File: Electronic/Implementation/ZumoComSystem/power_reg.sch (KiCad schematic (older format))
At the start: 16 parts, among them Q1 PMOS-RQ5C060BCTCL, SW1 MLL1200S, U1 LT1374CS8-5PBF, U2 TPS62056DGS

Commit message: Coutouts, BOM, ...
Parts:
- removed Q1: PMOS-RQ5C060BCTCL, footprints:SOT95P280X100-3N, symbol Device:Q_PMOS_GDS
- added Q1: PMOS_GSD-RQ5C060BCTCL, footprints:SOT95P280X100-3N, symbol Device:Q_PMOS_GSD
- C1, C3, C4: Manufacturer (none) -> TDK Corporation; Part-No. (none) -> C3216X5R1V226M160AC
- C2: Manufacturer (none) -> TDK Corporation; Part-No. (none) -> C2012X5R1V106M085AC
- C5: Manufacturer (none) -> KEMET; Part-No. (none) -> C0805C274K5RACTU
- C6: Manufacturer (none) -> TDK Corporation; Part-No. (none) -> C3216X5R1A107M160AC
- D1: Manufacturer (none) -> Kyocera AVX; Part-No. (none) -> SD2114S040S5R0
- D2: Manufacturer (none) -> SMC Diode Solutions; Part-No. (none) -> SD103BWSA
- L1: Manufacturer (none) -> Würth Elektronik; Part-No. (none) -> 74437368150
- L2: Manufacturer (none) -> Vishay Dale; Part-No. (none) -> IHLP6767GZER220M11
- R1: value 100k -> 10k; Manufacturer (none) -> TE Connectivity Passive Product; Part-No. (none) -> CRGCQ0603J10K
- R2: value 100k -> 68k; Manufacturer (none) -> TE Connectivity Passive Product; Part-No. (none) -> CRGCQ0603F68K
- SW1: Comment 1437575-1 -> (none); Manufacturer (none) -> TE Connectivity / P&B; Part-No. (none) -> MLL1200S
- U1: MANUFACTURER_PART_NUMBER lt1374cs85#pbf -> (none); Manufacturer (none) -> Analog Device; Part-No. (none) -> LT1374CS8-5PBF; VENDOR Linear Technology -> (none)
- U2: Manufacturer (none) -> Texas Instruments; Part-No. (none) -> TPS62056DGS

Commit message: replaced 3V3 Regulator
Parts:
- removed C3: 22uF, Capacitor_SMD:C_1206_3216Metric_Pad1.42x1.75mm_HandSolder, symbol Device:C
- removed U2: TPS62056DGS, SOP50P490X110-10N, symbol TPS62056DGS:TPS62056DGS
- added C6: 10u, Capacitor_SMD:C_0805_2012Metric_Pad1.15x1.40mm_HandSolder, symbol Device:C
- added R3: 10k, Resistor_SMD:R_0603_1608Metric_Pad1.05x0.95mm_HandSolder, symbol Device:R
- added U2: ADP2370ACPZ-3.3-R7, footprints:DFN300X300X80-9N_thermal, symbol 2022-04-19_08-29-50:ADP2370ACPZ-3.3-R7
- C2: value 10uF -> 10u
- L1: value 15uH -> 6.8u; footprint footprints:L_Wuerth_HCI-1040_3D -> Inductor_SMD:L_Coilcraft_XxL4040; Manufacturer Würth Elektronik -> Coilcraft; Part-No. 74437368150 -> XAL4030-682MEC
- renumbered C4 to C3, C5 to C4, C6 to C5
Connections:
- net +3V3: now also C6.1, U2.5 (FB)
- net GND: now also C6.2, U2.4 (SYNC), U2.8 (PGND), U2.9 (EPAD)
- net at C1.1, C2.1, C3.1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: now also R3.2, U2.1 (VIN), U2.2 (FSEL), U2.3 (EN)
- net at L1.1: now also U2.7 (SW)
- new net: R3.1, U2.6 (PG)
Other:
- note added: "Imax = 250mA"
- note removed: "Imax = 200 mA"
- moved on the sheet: L1

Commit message: actualized BOM
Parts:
- U2: Manufacturer (none) -> Analog Device; Part-No. (none) -> ADP2371ACPZ-3.3-R7
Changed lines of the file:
@@
 F 2 "footprints:DFN300X300X80-9N_thermal" H 6200 1640 60  0001 C CNN
 F 3 "https://www.analog.com/media/en/technical-documentation/data-sheets/ADP2370_2371.pdf" H 6200 1681 60  0001 C CNN
+F 4 "Analog Device" H 5000 1400 50  0001 C CNN "Manufacturer"
+F 5 "ADP2371ACPZ-3.3-R7" H 5000 1400 50  0001 C CNN "Part-No."
 	1    5000 1400
 	1    0    0    -1

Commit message: Electronic: ZumoCom System: finhished/ orderd PCB + add Version and TOP/BOT on PCB
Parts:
- C1: Manufacturer TDK Corporation -> Murata Electronics; Part-No. C3216X5R1V226M160AC -> GRM31CC81E226KE11L
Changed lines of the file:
@@
 Sheet 2 7
 Title "Zumo Communication System"
-Date "2022-04-22"
+Date "2022-05-13"
 Rev "V1.0"
 Comp "NewTec GmbH"
@@
 F 2 "Capacitor_SMD:C_1206_3216Metric_Pad1.42x1.75mm_HandSolder" H 3988 4700 50  0001 C CNN
 F 3 "https://product.tdk.com/info/en/catalog/datasheets/mlcc_commercial_general_en.pdf?ref_disty=digikey" H 3950 4850 50  0001 C CNN
-F 4 "TDK Corporation" H 3950 4850 50  0001 C CNN "Manufacturer"
-F 5 "C3216X5R1V226M160AC " H 3950 4850 50  0001 C CNN "Part-No."
+F 4 " Murata Electronics " H 3950 4850 50  0001 C CNN "Manufacturer"
+F 5 "GRM31CC81E226KE11L" H 3950 4850 50  0001 C CNN "Part-No."
 	1    3950 4850
 	1    0    0    -1

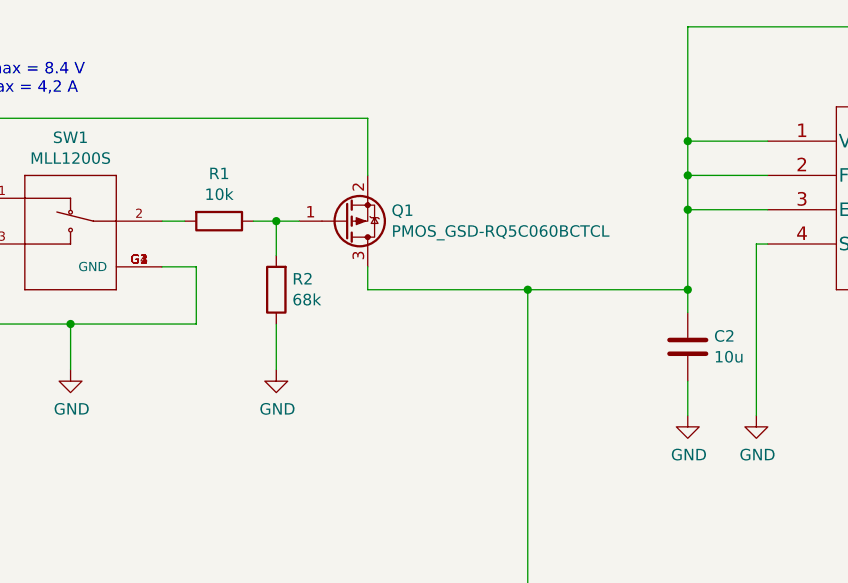
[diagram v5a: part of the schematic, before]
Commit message: #93 Voltage divider removed and another MOSFET Q1 selected
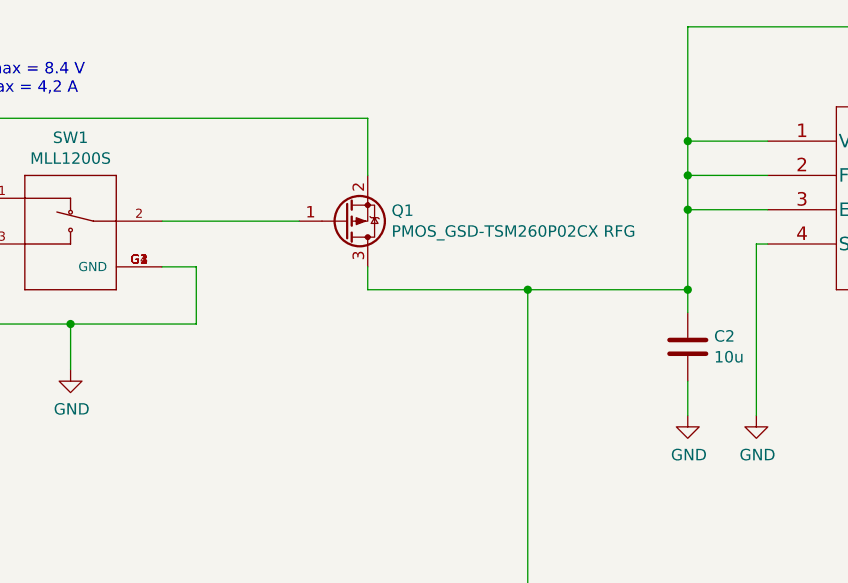
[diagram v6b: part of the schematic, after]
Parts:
- removed R1: 10k, Resistor_SMD:R_0603_1608Metric_Pad1.05x0.95mm_HandSolder, symbol Device:R
- removed R2: 68k, Resistor_SMD:R_0603_1608Metric_Pad1.05x0.95mm_HandSolder, symbol Device:R
- Q1: value PMOS_GSD-RQ5C060BCTCL -> PMOS_GSD-TSM260P02CX RFG; footprint footprints:SOT95P280X100-3N -> Package_TO_SOT_SMD:SOT-23_Handsoldering; Manufacturer Rohm Semiconductor -> Taiwan Semiconductor; Part-No. RQ5C060BCTCL -> TSM260P02CX RFG
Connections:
- net at SW1.2: now also Q1.1 (G)
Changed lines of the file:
@@
 	1000 1250 1450 1250
 Wire Wire Line
-	2350 1700 2450 1700
-Wire Wire Line
-	2750 1700 2850 1700
-Wire Wire Line
-	2850 2350 2850 2150
-Wire Wire Line
-	2850 1850 2850 1700
-$Comp
-L power:GND #PWR02
-U 1 1 62464A3F
-P 2850 2350
-F 0 "#PWR02" H 2850 2100 50  0001 C CNN
-F 1 "GND" H 2855 2177 50  0000 C CNN
-F 2 "" H 2850 2350 50  0001 C CNN
-F 3 "" H 2850 2350 50  0001 C CNN
-	1    2850 2350
-	1    0    0    -1
-$EndComp
-Wire Wire Line
 	3250 2000 3250 1900
 Wire Wire Line
 	3250 2000 3950 2000
-Wire Wire Line
-	2950 1700 2850 1700
-Connection ~ 2850 1700
 Wire Wire Line
 	3250 1250 3250 1500
@@
 $EndComp
 $Comp
-L Device:R R1
-U 1 1 62459142
-P 2600 1700
-F 0 "R1" V 2393 1700 50  0000 C CNN
-F 1 "10k" V 2484 1700 50  0000 C CNN
-F 2 "Resistor_SMD:R_0603_1608Metric_Pad1.05x0.95mm_HandSolder" V 2530 1700 50  0001 C CNN
-F 3 "~" H 2600 1700 50  0001 C CNN
-F 4 "TE Connectivity Passive Product" H 2600 1700 50  0001 C CNN "Manufacturer"
-F 5 "CRGCQ0603J10K" H 2600 1700 50  0001 C CNN "Part-No."
-	1    2600 1700
-	0    1    1    0
-$EndComp
-$Comp
-L Device:R R2
-U 1 1 6245A145
-P 2850 2000
-F 0 "R2" H 2780 1954 50  0000 R CNN
-F 1 "68k" H 2780 2045 50  0000 R CNN
-F 2 "Resistor_SMD:R_0603_1608Metric_Pad1.05x0.95mm_HandSolder" V 2780 2000 50  0001 C CNN
-F 3 "~" H 2850 2000 50  0001 C CNN
-F 4 "TE Connectivity Passive Product" H 2850 2000 50  0001 C CNN "Manufacturer"
-F 5 "CRGCQ0603F68K" H 2850 2000 50  0001 C CNN "Part-No."
-	1    2850 2000
-	-1   0    0    1
-$EndComp
-$Comp
 L Device:L L1
 U 1 1 60C698F7
@@
 P 3150 1700
 F 0 "Q1" H 3354 1654 50  0000 L CNN
-F 1 "PMOS_GSD-RQ5C060BCTCL" H 3354 1745 50  0000 L CNN
-F 2 "footprints:SOT95P280X100-3N" H 3350 1800 50  0001 C CNN
-F 3 "https://fscdn.rohm.com/en/products/databook/datasheet/discrete/transistor/mosfet/rq5c060bctcl-e.pdf" H 3150 1700 50  0001 C CNN
-F 4 "Rohm Semiconductor" H 3150 1700 50  0001 C CNN "Manufacturer"
-F 5 "RQ5C060BCTCL" H 3150 1700 50  0001 C CNN "Part-No."
+F 1 "PMOS_GSD-TSM260P02CX RFG " H 3354 1745 50  0000 L CNN
+F 2 "Package_TO_SOT_SMD:SOT-23_Handsoldering" H 3350 1800 50  0001 C CNN
+F 3 "https://www.mouser.de/datasheet/2/395/TSM260P02_D1811-1918704.pdf" H 3150 1700 50  0001 C CNN
+F 4 "Taiwan Semiconductor " H 3150 1700 50  0001 C CNN "Manufacturer"
+F 5 "TSM260P02CX RFG " H 3150 1700 50  0001 C CNN "Part-No."
 	1    3150 1700
 	1    0    0    1
@@
 	1    0    0    -1
 $EndComp
+Wire Wire Line
+	2350 1700 2950 1700
 $EndSCHEMATC

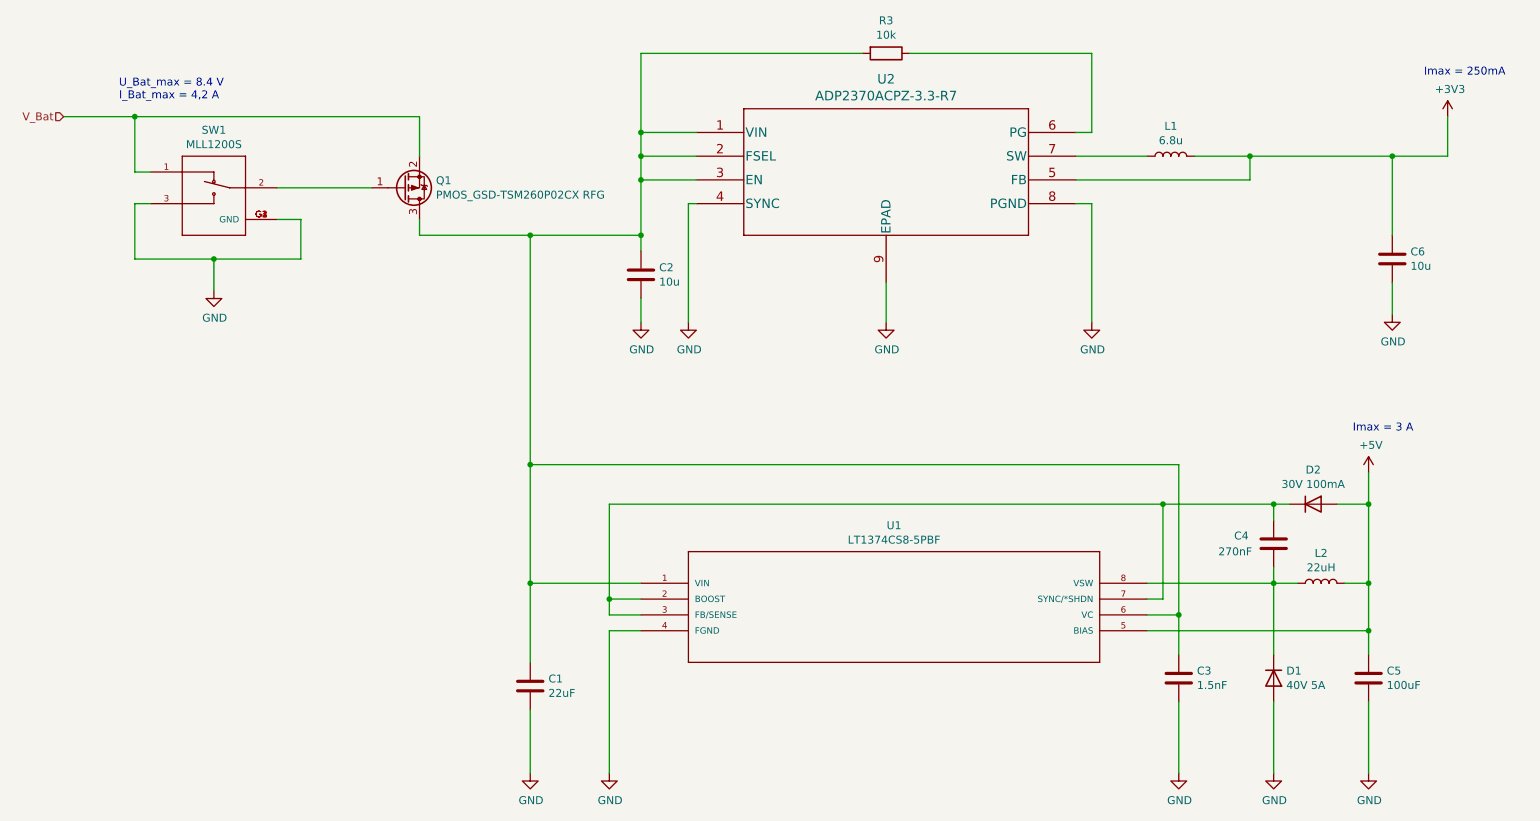
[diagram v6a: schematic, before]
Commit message: #93 5V voltage regulator /SHDN; L2 select; FB/SENSE;VC
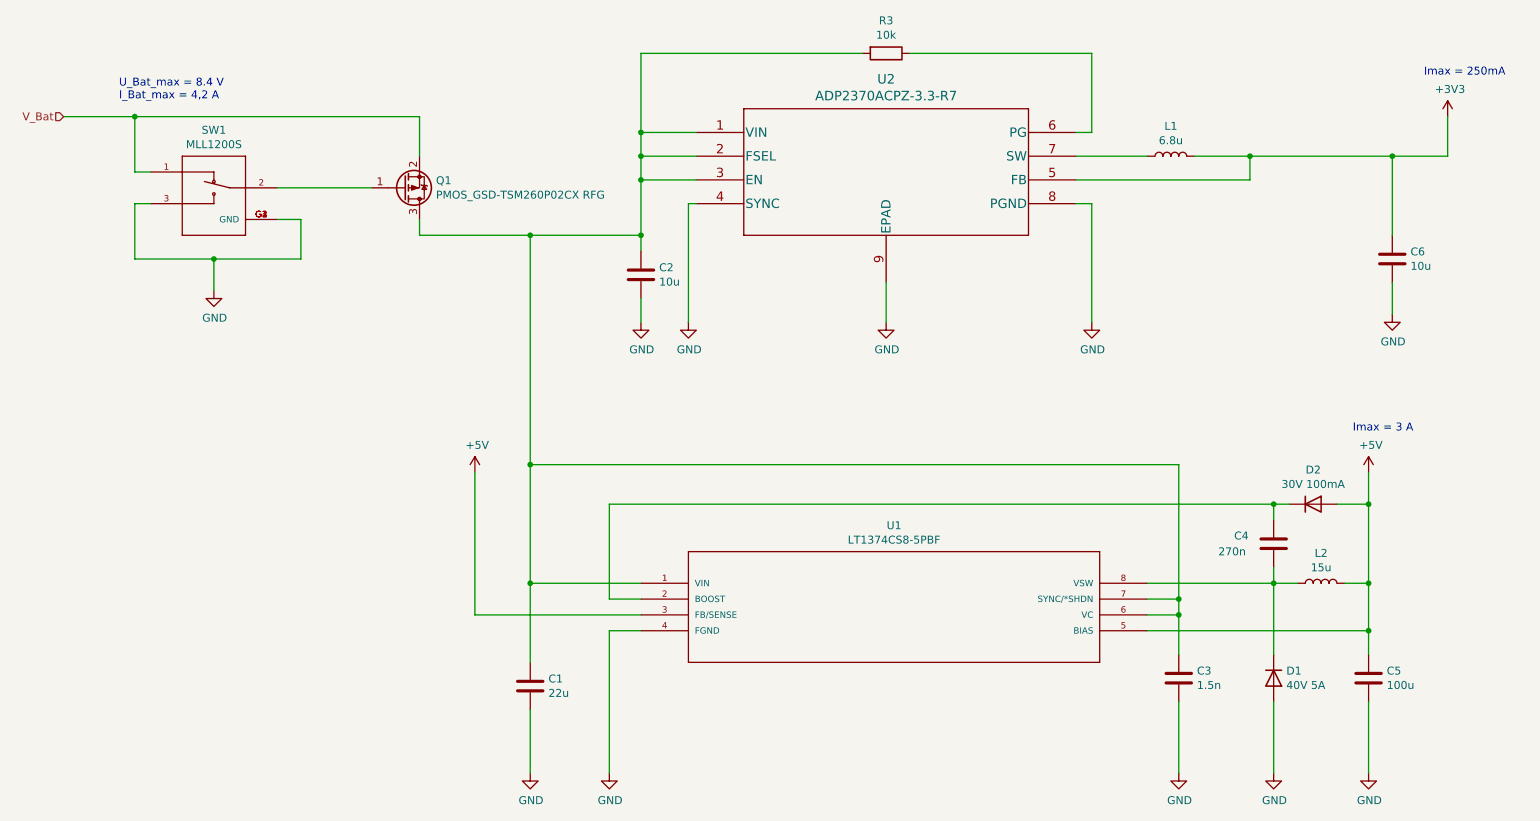
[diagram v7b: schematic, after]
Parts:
- C1: value 22uF -> 22u
- C3: value 1.5nF -> 1.5n
- C4: value 270nF -> 270n
- C5: value 100uF -> 100u
- L2: value 22uH -> 15u; footprint footprints:L_Wuerth_HCI-1350_3D -> Inductor_SMD:L_Vishay_IHLP-4040; Manufacturer Vishay Dale -> Vishay / Dale; Part-No. IHLP6767GZER220M11 -> IHLP4040DZER150M5A
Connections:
- net +5V: now also U1.3 (FB/SENSE)
- net at C1.1, C2.1, C3.1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: now also U1.7 (SYNC/*SHDN)
- net at C4.1, D2.1 (K), U1.2 (BOOST): no longer U1.3 (FB/SENSE), U1.7 (SYNC/*SHDN)
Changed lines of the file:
@@
 	8650 3700 8650 3800
 Wire Wire Line
-	8650 3700 7950 3700
-Wire Wire Line
 	4450 3700 4450 4300
-Connection ~ 8650 3700
-Wire Wire Line
-	4650 4400 4450 4400
-Wire Wire Line
-	4450 4400 4450 4300
-Connection ~ 4450 4300
 Wire Wire Line
 	9250 4500 9250 4200
@@
 Wire Wire Line
 	9250 4950 9250 5400
-Wire Wire Line
-	3950 3450 8050 3450
 Connection ~ 9250 3700
 Wire Wire Line
@@
 	4450 4500 4650 4500
 Wire Wire Line
-	7850 4300 7950 4300
-Wire Wire Line
-	7950 4300 7950 3700
-Connection ~ 7950 3700
-Wire Wire Line
-	7950 3700 4450 3700
-Wire Wire Line
-	8050 3450 8050 4400
+	8050 3450 8050 4300
 Wire Wire Line
 	3950 2000 3950 3450
@@
 P 3950 4850
 F 0 "C1" H 4065 4896 50  0000 L CNN
-F 1 "22uF" H 4065 4805 50  0000 L CNN
+F 1 "22u" H 4065 4805 50  0000 L CNN
 F 2 "Capacitor_SMD:C_1206_3216Metric_Pad1.42x1.75mm_HandSolder" H 3988 4700 50  0001 C CNN
 F 3 "https://product.tdk.com/info/en/catalog/datasheets/mlcc_commercial_general_en.pdf?ref_disty=digikey" H 3950 4850 50  0001 C CNN
@@
 P 8050 4800
 F 0 "C3" H 8165 4846 50  0000 L CNN
-F 1 "1.5nF" H 8165 4755 50  0000 L CNN
+F 1 "1.5n" H 8165 4755 50  0000 L CNN
 F 2 "Capacitor_SMD:C_0603_1608Metric_Pad1.05x0.95mm_HandSolder" H 8088 4650 50  0001 C CNN
 F 3 "https://www.we-online.de/katalog/datasheet/885012206084.pdf" H 8050 4800 50  0001 C CNN
@@
 P 9250 4800
 F 0 "C5" H 9365 4846 50  0000 L CNN
-F 1 "100uF" H 9365 4755 50  0000 L CNN
+F 1 "100u" H 9365 4755 50  0000 L CNN
 F 2 "Capacitor_SMD:C_1206_3216Metric_Pad1.42x1.75mm_HandSolder" H 9288 4650 50  0001 C CNN
 F 3 "https://product.tdk.com/en/system/files?file=dam/doc/product/capacitor/ceramic/mlcc/catalog/mlcc_commercial_general_en.pdf" H 9250 4800 50  0001 C CNN
@@
 P 8950 4200
 F 0 "L2" V 9140 4200 50  0000 C CNN
-F 1 "22uH" V 9049 4200 50  0000 C CNN
-F 2 "footprints:L_Wuerth_HCI-1350_3D" H 8950 4200 50  0001 C CNN
-F 3 "https://www.vishay.com/docs/34282/ihlp-6767gz-11.pdf" H 8950 4200 50  0001 C CNN
-F 4 "Vishay Dale" H 8950 4200 50  0001 C CNN "Manufacturer"
-F 5 "IHLP6767GZER220M11" H 8950 4200 50  0001 C CNN "Part-No."
+F 1 "15u" V 9049 4200 50  0000 C CNN
+F 2 "Inductor_SMD:L_Vishay_IHLP-4040" H 8950 4200 50  0001 C CNN
+F 3 "https://www.mouser.de/datasheet/2/427/lp40dz5a-1762293.pdf" H 8950 4200 50  0001 C CNN
+F 4 " Vishay / Dale " H 8950 4200 50  0001 C CNN "Manufacturer"
+F 5 "IHLP4040DZER150M5A" H 8950 4200 50  0001 C CNN "Part-No."
 	1    8950 4200
 	0    -1   -1   0
@@
 P 8650 3950
 F 0 "C4" H 8400 4000 50  0000 L CNN
-F 1 "270nF" H 8300 3900 50  0000 L CNN
+F 1 "270n" H 8300 3900 50  0000 L CNN
 F 2 "Capacitor_SMD:C_0805_2012Metric_Pad1.15x1.40mm_HandSolder" H 8688 3800 50  0001 C CNN
 F 3 "https://api.kemet.com/component-edge/download/specsheet/C0805R274K5RACT500.pdf" H 8650 3950 50  0001 C CNN
@@
 Wire Wire Line
 	2350 1700 2950 1700
+Wire Wire Line
+	3950 3450 8050 3450
+Wire Wire Line
+	7850 4300 8050 4300
+Connection ~ 8050 4300
+Wire Wire Line
+	8050 4300 8050 4400
+Connection ~ 8650 3700
+Wire Wire Line
+	4450 3700 8650 3700
+$Comp
+L power:+5V #PWR?
+U 1 1 62EA39DD
+P 3600 3500
+F 0 "#PWR?" H 3600 3350 50  0001 C CNN
+F 1 "+5V" H 3615 3673 50  0000 C CNN
+F 2 "" H 3600 3500 50  0001 C CNN
+F 3 "" H 3600 3500 50  0001 C CNN
+	1    3600 3500
+	1    0    0    -1
+$EndComp
+Wire Wire Line
+	3600 3500 3600 4400
+Wire Wire Line
+	3600 4400 4650 4400
 $EndSCHEMATC

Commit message: #93 3V3 voltage regulator increased footprint size from L1 (for better soldering)
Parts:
- L1: footprint Inductor_SMD:L_Coilcraft_XxL4040 -> footprints:L_Coilcraft_XxL4040_Handsolder
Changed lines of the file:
@@
 F 0 "L1" V 8190 1500 50  0000 C CNN
 F 1 "6.8u" V 8099 1500 50  0000 C CNN
-F 2 "Inductor_SMD:L_Coilcraft_XxL4040" H 8000 1500 50  0001 C CNN
+F 2 "footprints:L_Coilcraft_XxL4040_Handsolder" H 8000 1500 50  0001 C CNN
 F 3 "https://www.mouser.de/datasheet/2/597/xal4000-270751.pdf" H 8000 1500 50  0001 C CNN
 F 4 "Coilcraft" H 8000 1500 50  0001 C CNN "Manufacturer"
